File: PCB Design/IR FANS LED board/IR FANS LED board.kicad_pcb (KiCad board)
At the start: 2 copper layers, 148.7 x 29 mm, 9 parts, among them J1 Fans, J2 Fans, J3 IR, J4 Fans from above, J5 IR, J6 IR from above, J7 IR, J8 Fans, J9 Fans

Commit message: Zachary IR and RGW LED boards revisions
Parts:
- moved J6 7.03 mm to (168.7, 32.3)
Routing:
- net /IR LED+: track 90.0 -> 80.5 mm
- net /IR LED-: track 87.8 -> 79.6 mm
- net /HV5: track 184.6 -> 190.5 mm
- net /X: track 175.7 -> 179.2 mm
- net /12V: track 164.0 -> 167.2 mm
- net /GND: track 150.8 -> 153.7 mm

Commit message: Gerber Files
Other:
- board text added: "Bottom Box IR and Fans Panel"
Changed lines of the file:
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@@
       (layerselection 0x00010fc_ffffffff)
       (disableapertmacros false)
-      (usegerberextensions false)
-      (usegerberattributes true)
+      (usegerberextensions true)
+      (usegerberattributes false)
       (usegerberadvancedattributes true)
-      (creategerberjobfile true)
+      (creategerberjobfile false)
       (svguseinch false)
       (svgprecision 6)
@@
       (outputformat 1)
       (mirror false)
-      (drillshape 1)
+      (drillshape 0)
       (scaleselection 1)
-      (outputdirectory "")
+      (outputdirectory "../IRGerber/")
     )
   )
@@
   )
   (gr_rect (start 60.3504 18.1864) (end 209.0928 47.1932) (layer "Edge.Cuts") (width 0.1) (fill none))
+  (gr_text "Bottom Box IR and Fans Panel" (at 133.35 32.385) (layer "F.SilkS")
+    (effects (font (size 1 1) (thickness 0.15)))
+  )
   (segment (start 175.006 20.32) (end 173.482 21.844) (width 0.635) (layer "F.Cu") (net 1))
   (segment (start 68.58 43.18) (end 62.738 37.338) (width 0.635) (layer "F.Cu") (net 1))

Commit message: Logos and labels
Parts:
- added G***: LOGO, LOGO, F.Cu at (186.1, 36.8)
- added G***: LOGO, LOGO, F.Cu at (85.1, 41.9)
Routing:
- net /IR LED-: track 79.6 -> 92.3 mm
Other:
- board text added: "Flybox IR and Fans Board"
- board text added: "Made for the Rosbash Lab at Brandeis By the 2022-23 Olin College SCOPE team"

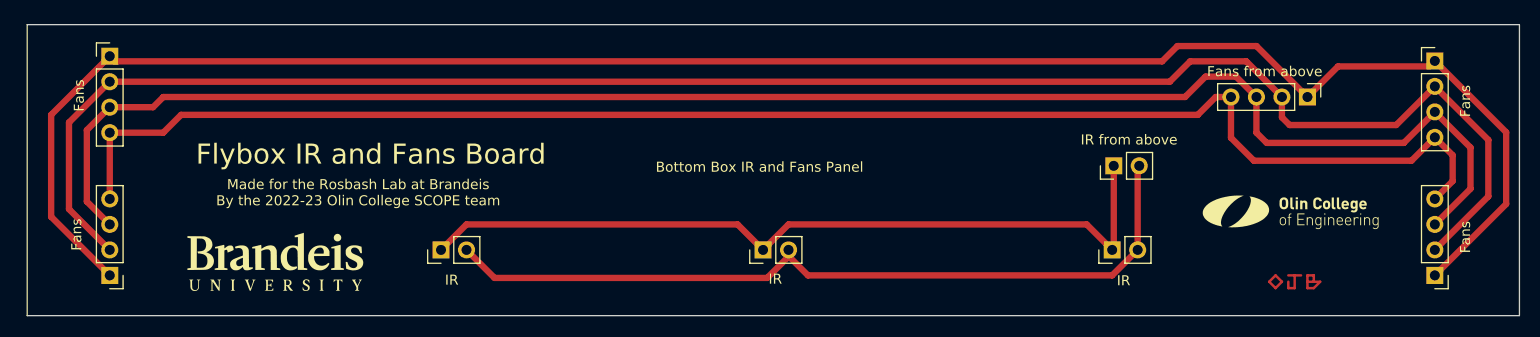
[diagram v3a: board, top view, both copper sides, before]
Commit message: V2 IR and RGW boards done
Main board missing button footprint
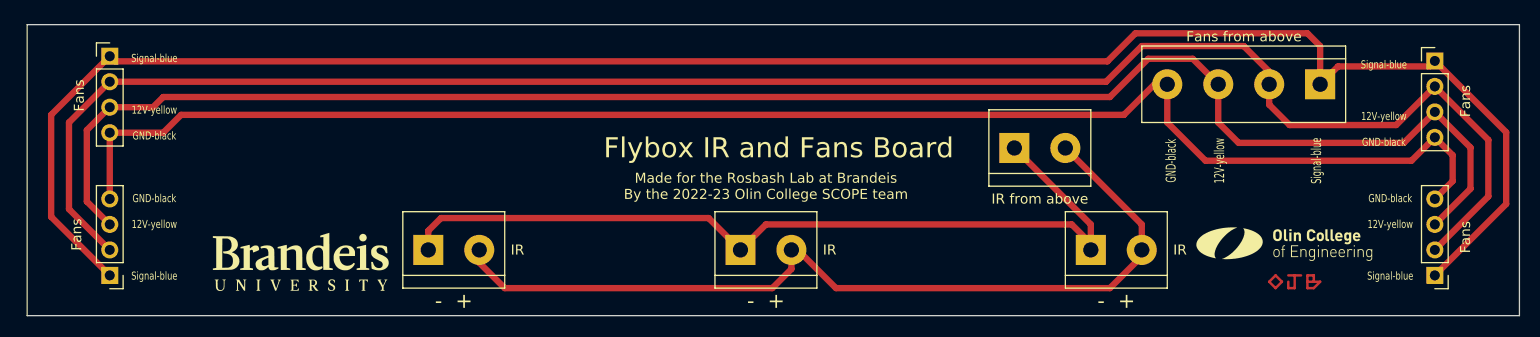
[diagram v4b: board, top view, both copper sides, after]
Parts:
- J3, J5, J6, J7: footprint Connector_PinHeader_2.54mm:PinHeader_1x02_P2.54mm_Vertical -> TerminalBlock:TerminalBlock_bornier-2_P5.08mm
- J4: footprint Connector_PinHeader_2.54mm:PinHeader_1x04_P2.54mm_Vertical -> TerminalBlock:TerminalBlock_bornier-4_P5.08mm
- moved J6 10.1 mm to (158.8, 30.5), turned to 0 degrees
- moved G*** 3.24 mm to (185.4, 40.0)
- moved G*** 2.54 mm to (87.6, 41.9)
- moved J3 2.26 mm to (131.4, 40.6), turned to 0 degrees
- moved J5 2.13 mm to (166.4, 40.6), turned to 0 degrees
- moved J4 1.80 mm to (189.2, 24.1), turned to 180 degrees
- moved J7 1.27 mm to (100.3, 40.6), turned to 0 degrees
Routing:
- net (no net): track 0.00 -> 12.7 mm
- net /IR LED+: track 80.5 -> 87.9 mm
- net /IR LED-: track 92.3 -> 85.6 mm
- net /HV5: track 190.5 -> 192.7 mm
- net /X: track 179.2 -> 181.2 mm
- net /12V: track 167.2 -> 168.8 mm
- net /GND: track 153.7 -> 154.6 mm
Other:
- board text added: "- +"
- board text added: "GND-black 12V-yellow Signal-blue"
- board text added: "Signal-blue 12V-yellow GND-black"
- board text removed: "Bottom Box IR and Fans Panel"

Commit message: Finished V2 PCBs with rounded edges
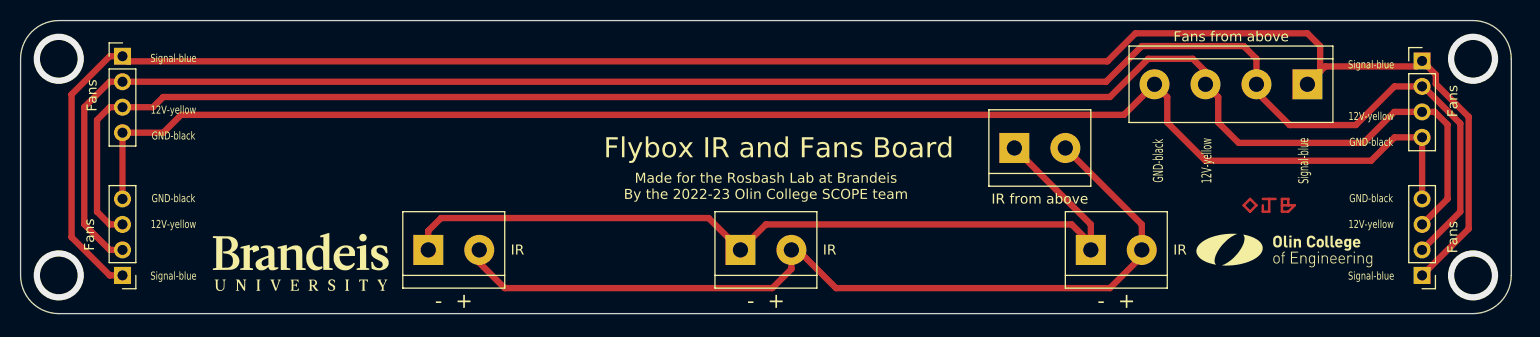
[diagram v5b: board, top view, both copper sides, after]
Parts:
- moved J1 1.27 mm to (199.4, 21.8)
- moved J8 1.27 mm to (199.4, 43.2)
- moved J2 1.27 mm to (69.8, 21.3)
- moved J9 1.27 mm to (69.8, 43.2)
- moved J4 1.27 mm to (188.0, 24.1)
- moved G*** 0.63 mm to (185.4, 40.6)
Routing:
- net /GND: track 154.6 -> 149.9 mm
- net /X: track 181.2 -> 178.7 mm
- net /HV5: track 192.7 -> 190.8 mm
- net /12V: track 168.8 -> 167.9 mm
- net (no net): vias 0 -> 4
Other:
- board size 148.7 x 29 mm -> 148.6 x 29.2 mm

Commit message: Shrunk vias, fixed ohms and XV1 labels
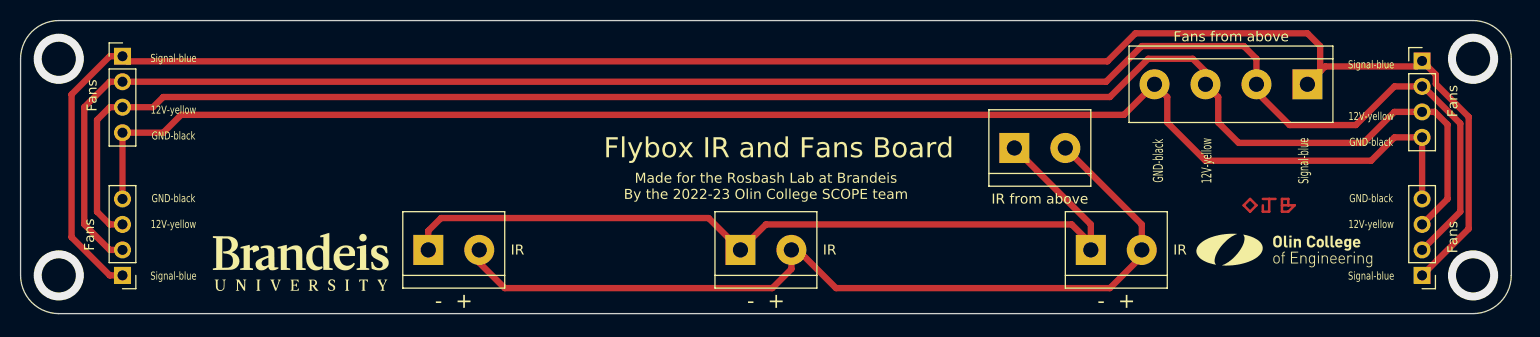
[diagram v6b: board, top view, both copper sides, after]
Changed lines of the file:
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@@
   (segment (start 182.245 36.83) (end 181.61 36.195) (width 0.25) (layer "F.Cu") (net 0))
   (segment (start 186.055 35.56) (end 186.055 36.195) (width 0.25) (layer "F.Cu") (net 0))
-  (via (at 204.47 21.59) (size 5) (drill 3.75) (layers "F.Cu" "B.Cu") (free) (net 0))
-  (via (at 204.47 43.18) (size 5) (drill 3.75) (layers "F.Cu" "B.Cu") (free) (net 0))
-  (via (at 63.5 43.18) (size 5) (drill 3.75) (layers "F.Cu" "B.Cu") (free) (net 0))
-  (via (at 63.5 21.59) (size 5) (drill 3.75) (layers "F.Cu" "B.Cu") (free) (net 0))
+  (via (at 204.47 21.59) (size 5) (drill 3.4) (layers "F.Cu" "B.Cu") (free) (net 0))
+  (via (at 204.47 43.18) (size 5) (drill 3.4) (layers "F.Cu" "B.Cu") (free) (net 0))
+  (via (at 63.5 43.18) (size 5) (drill 3.4) (layers "F.Cu" "B.Cu") (free) (net 0))
+  (via (at 63.5 21.59) (size 5) (drill 3.4) (layers "F.Cu" "B.Cu") (free) (net 0))
   (segment (start 199.39 21.8032) (end 200.7575 23.1707) (width 0.635) (layer "F.Cu") (net 1))
   (segment (start 64.77 25.146) (end 68.58 21.336) (width 0.635) (layer "F.Cu") (net 1))

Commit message: Zachary review of IR and RGW and Fans boards
@oliviajobradley All done reviewing all three boards. I played with the silkscreen a bit, not sure if it's better or worse. OJ, feel free to change it back if you'd prefer.

Let's order!
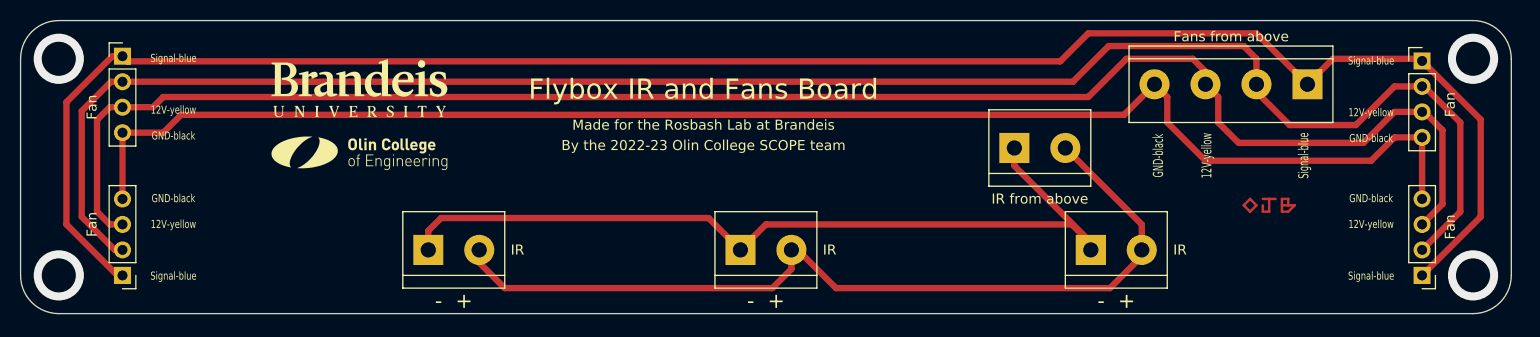
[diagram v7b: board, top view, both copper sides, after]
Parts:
- J1, J2, J8, J9: value Fans -> Fan
- moved G*** 92.7 mm to (93.2, 30.9)
- moved G*** 18.3 mm to (93.5, 24.6)
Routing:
- net /HV5: track 190.8 -> 187.7 mm
- net /12V: track 167.9 -> 166.8 mm
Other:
- board text added: "By the 2022-23 Olin College SCOPE team"
- board text added: "Made for the Rosbash Lab at Brandeis"
- board text removed: "Made for the Rosbash Lab at Brandeis By the 2022-23 Olin College SCOPE team"

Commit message: A few more PCB edits
- Eliminated and/or shortened traces on rear side (no more long traces on the rear side)
- Connected four screw vias on IR board to GND
- Ran DRC on all boards and addressed issues where necessary

Imo, we should be ready to order on @oliviajobradley's approval.
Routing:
- net /GND: track 149.9 -> 235.6 mm, vias 0 -> 4
- net (no net): vias 4 -> 0
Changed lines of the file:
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@@
   (segment (start 182.245 36.83) (end 181.61 36.195) (width 0.25) (layer "F.Cu") (net 0))
   (segment (start 186.055 35.56) (end 186.055 36.195) (width 0.25) (layer "F.Cu") (net 0))
-  (via (at 204.47 21.59) (size 5) (drill 3.4) (layers "F.Cu" "B.Cu") (free) (net 0))
-  (via (at 204.47 43.18) (size 5) (drill 3.4) (layers "F.Cu" "B.Cu") (free) (net 0))
-  (via (at 63.5 43.18) (size 5) (drill 3.4) (layers "F.Cu" "B.Cu") (free) (net 0))
-  (via (at 63.5 21.59) (size 5) (drill 3.4) (layers "F.Cu" "B.Cu") (free) (net 0))
   (segment (start 64.262 38.1) (end 64.262 25.908) (width 0.635) (layer "F.Cu") (net 1))
-  (segment (start 199.39 21.8032) (end 205.232 27.6452) (width 0.635) (layer "F.Cu") (net 1))
   (segment (start 199.1768 21.59) (end 199.39 21.8032) (width 0.635) (layer "F.Cu") (net 1))
   (segment (start 70.358 21.844) (end 69.85 21.336) (width 0.635) (layer "F.Cu") (net 1))
-  (segment (start 205.232 27.6452) (end 205.232 37.338) (width 0.635) (layer "F.Cu") (net 1))
   (segment (start 190.5 21.59) (end 199.1768 21.59) (width 0.635) (layer "F.Cu") (net 1))
   (segment (start 166.116 19.05) (end 163.322 21.844) (width 0.635) (layer "F.Cu") (net 1))
@@
   (segment (start 187.96 24.13) (end 190.5 21.59) (width 0.635) (layer "F.Cu") (net 1))
   (segment (start 68.834 21.336) (end 69.85 21.336) (width 0.635) (layer "F.Cu") (net 1))
-  (segment (start 205.232 37.338) (end 199.39 43.18) (width 0.635) (layer "F.Cu") (net 1))
+  (segment (start 204.978 37.592) (end 199.39 43.18) (width 0.635) (layer "F.Cu") (net 1))
   (segment (start 182.88 19.05) (end 166.116 19.05) (width 0.635) (layer "F.Cu") (net 1))
   (segment (start 64.262 25.908) (end 68.834 21.336) (width 0.635) (layer "F.Cu") (net 1))
   (segment (start 187.96 24.13) (end 182.88 19.05) (width 0.635) (layer "F.Cu") (net 1))
   (segment (start 69.342 43.18) (end 64.262 38.1) (width 0.635) (layer "F.Cu") (net 1))
+  (segment (start 199.39 21.8032) (end 204.978 27.3912) (width 0.635) (layer "F.Cu") (net 1))
+  (segment (start 204.978 27.3912) (end 204.978 37.592) (width 0.635) (layer "F.Cu") (net 1))
   (segment (start 69.088 40.64) (end 69.85 40.64) (width 0.635) (layer "F.Cu") (net 2))
   (segment (start 203.2 27.94) (end 203.2 36.83) (width 0.635) (layer "F.Cu") (net 2))
@@
   (segment (start 72.898 26.416) (end 73.914 25.4) (width 0.635) (layer "F.Cu") (net 3))
   (segment (start 201.422 36.068) (end 199.39 38.1) (width 0.635) (layer "F.Cu") (net 3))
+  (segment (start 63.5 21.59) (end 62.484 22.606) (width 0.635) (layer "F.Cu") (net 4))
+  (segment (start 198.374 45.466) (end 202.184 45.466) (width 0.635) (layer "F.Cu") (net 4))
   (segment (start 173.99 27.94) (end 177.8 31.75) (width 0.635) (layer "F.Cu") (net 4))
+  (segment (start 71.12 45.72) (end 72.644 44.196) (width 0.635) (layer "F.Cu") (net 4))
+  (segment (start 204.47 21.59) (end 206.756 23.876) (width 0.635) (layer "F.Cu") (net 4))
   (segment (start 173.99 25.4) (end 173.99 27.94) (width 0.635) (layer "F.Cu") (net 4))
+  (segment (start 198.628 35.56) (end 196.85 37.338) (width 0.635) (layer "F.Cu") (net 4))
   (segment (start 69.85 28.956) (end 73.914 28.956) (width 0.635) (layer "F.Cu") (net 4))
+  (segment (start 72.644 44.196) (end 72.644 37.084) (width 0.635) (layer "F.Cu") (net 4))
+  (segment (start 62.484 22.606) (end 62.484 42.164) (width 0.635) (layer "F.Cu") (net 4))
+  (segment (start 196.85 43.942) (end 198.374 45.466) (width 0.635) (layer "F.Cu") (net 4))
+  (segment (start 206.756 23.876) (end 206.756 40.894) (width 0.635) (layer "F.Cu") (net 4))
   (segment (start 69.85 28.956) (end 69.85 35.56) (width 0.635) (layer "F.Cu") (net 4))
+  (segment (start 72.644 37.084) (end 71.12 35.56) (width 0.635) (layer "F.Cu") (net 4))
   (segment (start 73.914 28.956) (end 75.692 27.178) (width 0.635) (layer "F.Cu") (net 4))
   (segment (start 75.692 27.178) (end 169.672 27.178) (width 0.635) (layer "F.Cu") (net 4))
@@
   (segment (start 194.31 31.75) (end 196.6368 29.4232) (width 0.635) (layer "F.Cu") (net 4))
   (segment (start 177.8 31.75) (end 194.31 31.75) (width 0.635) (layer "F.Cu") (net 4))
+  (segment (start 62.484 42.164) (end 63.5 43.18) (width 0.635) (layer "F.Cu") (net 4))
+  (segment (start 206.756 40.894) (end 204.47 43.18) (width 0.635) (layer "F.Cu") (net 4))
   (segment (start 196.6368 29.4232) (end 199.39 29.4232) (width 0.635) (layer "F.Cu") (net 4))
+  (segment (start 196.85 37.338) (end 196.85 43.942) (width 0.635) (layer "F.Cu") (net 4))
   (segment (start 169.672 27.178) (end 172.72 24.13) (width 0.635) (layer "F.Cu") (net 4))
+  (segment (start 202.184 45.466) (end 204.015684 43.634316) (width 0.635) (layer "F.Cu") (net 4))
+  (segment (start 71.12 35.56) (end 69.85 35.56) (width 0.635) (layer "F.Cu") (net 4))
+  (segment (start 63.5 43.18) (end 66.04 45.72) (width 0.635) (layer "F.Cu") (net 4))
   (segment (start 172.72 24.13) (end 173.99 25.4) (width 0.635) (layer "F.Cu") (net 4))
+  (segment (start 66.04 45.72) (end 71.12 45.72) (width 0.635) (layer "F.Cu") (net 4))
+  (segment (start 199.39 35.56) (end 198.628 35.56) (width 0.635) (layer "F.Cu") (net 4))
+  (via (at 204.47 21.59) (size 5) (drill 3.4) (layers "F.Cu" "B.Cu") (free) (net 4))
+  (via (at 204.47 43.18) (size 5) (drill 3.4) (layers "F.Cu" "B.Cu") (free) (net 4))
+  (via (at 63.5 43.18) (size 5) (drill 3.4) (layers "F.Cu" "B.Cu") (free) (net 4))
+  (via (at 63.5 21.59) (size 5) (drill 3.4) (layers "F.Cu" "B.Cu") (free) (net 4))
   (segment (start 158.75 32.258) (end 158.75 30.48) (width 0.635) (layer "F.Cu") (net 5))
   (segment (start 164.465 38.1) (end 166.37 40.005) (width 0.635) (layer "F.Cu") (net 5))
